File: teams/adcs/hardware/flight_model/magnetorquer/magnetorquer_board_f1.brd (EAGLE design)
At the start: 90 x 90 mm, 58 parts, among them U5 LTC3624

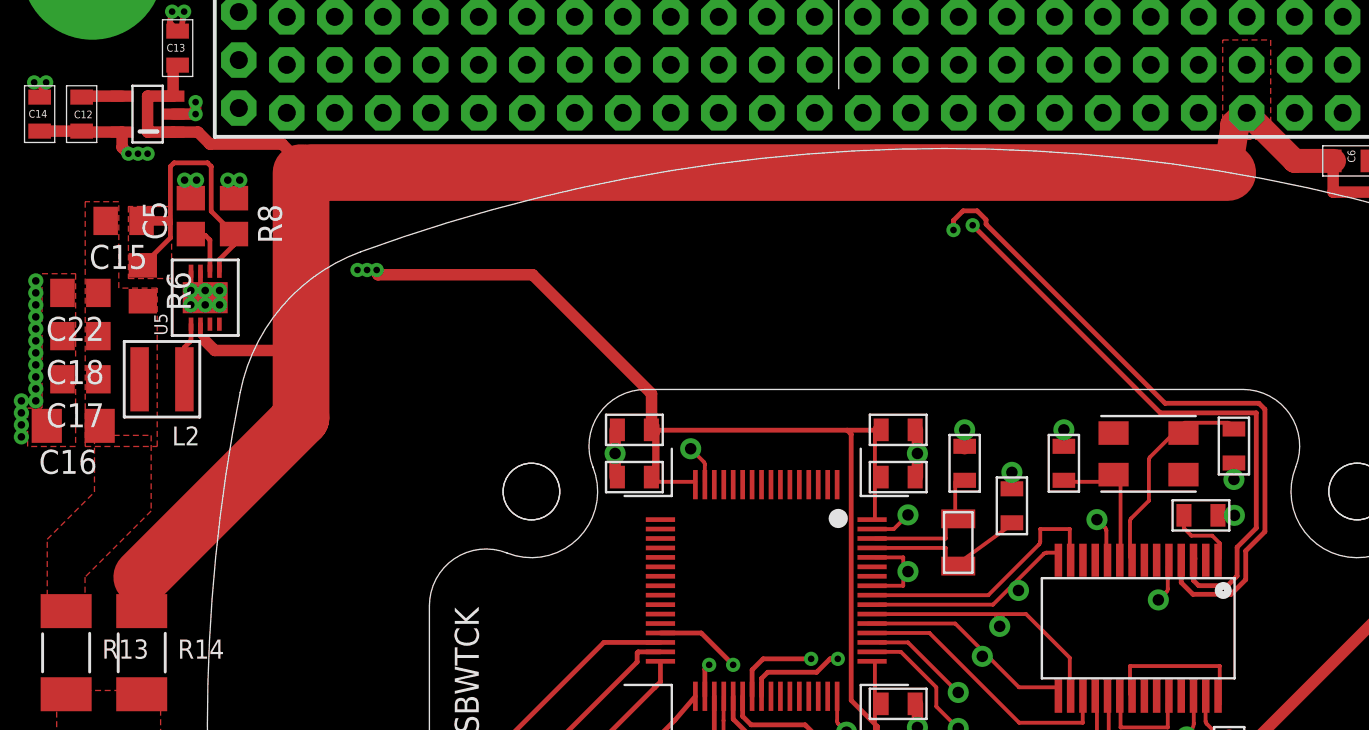
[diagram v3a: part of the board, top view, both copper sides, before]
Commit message: ADCS/MT: Add input capacitance on buck converter
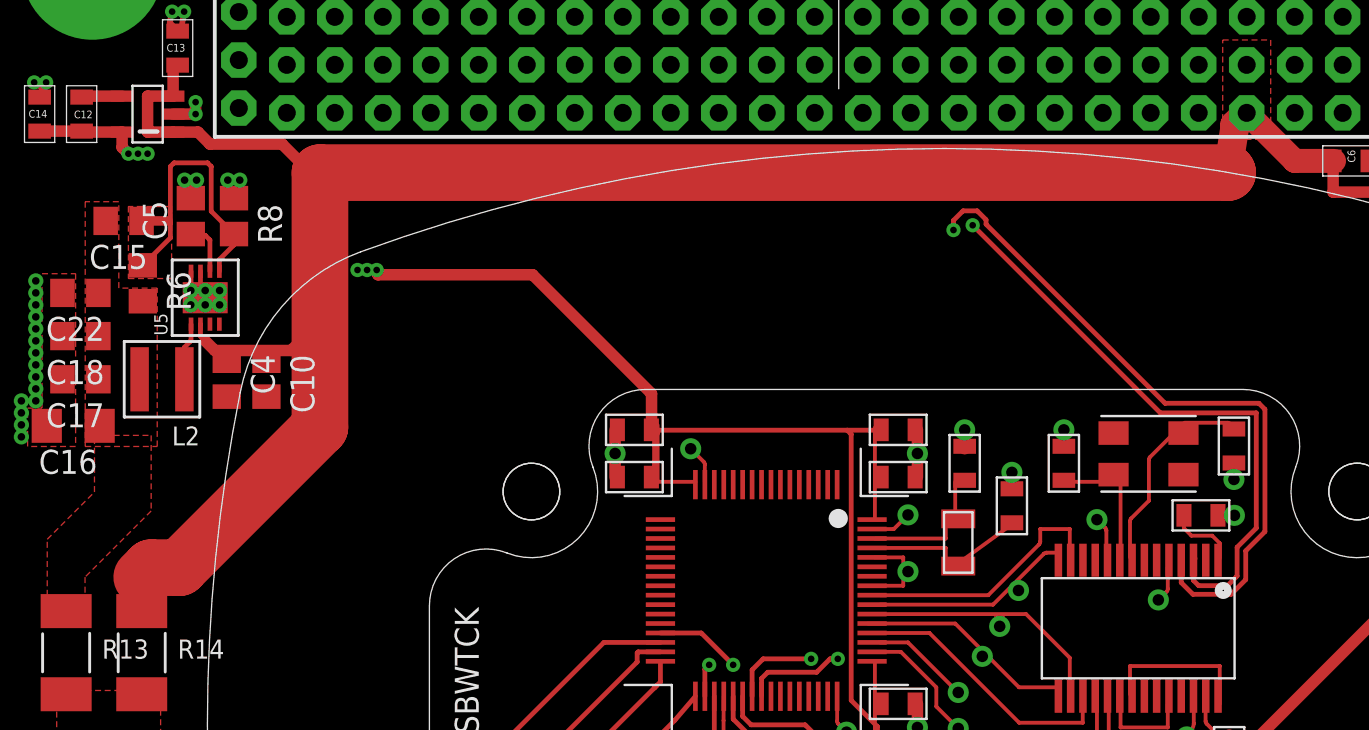
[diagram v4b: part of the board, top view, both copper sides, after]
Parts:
- added C10: 10µF, rcl:C0805
- added C4: 1µF, rcl:C0805
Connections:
- net GND: now also C10.2, C4.2
- net VBAT: now also C10.1, C4.1
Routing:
- net VBAT: track 124.1 -> 126.7 mm
- net +3V3: track 86.1 -> 83.8 mm
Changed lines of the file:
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@@
 <?xml version="1.0" encoding="utf-8"?>
 <!DOCTYPE eagle SYSTEM "eagle.dtd">
-<eagle version="8.4.2">
+<eagle version="9.0.0">
 <drawing>
 <settings>
@@
 <param name="checkRestrict" value="1"/>
 <param name="checkStop" value="0"/>
+<param name="checkValues" value="0"/>
 <param name="useDiameter" value="13"/>
 <param name="maxErrors" value="50"/>
@@
 <element name="R13" library="DubSat1 Components" package="R2010" value="0" x="15.5" y="47" rot="R270"/>
 <element name="R14" library="DubSat1 Components" package="R2010" value="DNP" x="19.5" y="47" rot="R270"/>
+<element name="C4" library="rcl" library_urn="urn:adsk.eagle:library:334" package="C0805" package3d_urn="urn:adsk.eagle:package:23617/2" value="1µF" x="24" y="61.5" rot="R270">
+<attribute name="SPICEPREFIX" value="C" x="24" y="61.5" size="1.778" layer="27" rot="R270" display="off"/>
+</element>
+<element name="C10" library="rcl" library_urn="urn:adsk.eagle:library:334" package="C0805" package3d_urn="urn:adsk.eagle:package:23617/2" value="10µF" x="26.1" y="61.5" rot="R270">
+<attribute name="SPICEPREFIX" value="C" x="26.1" y="61.5" size="1.778" layer="27" rot="R270" display="off"/>
+</element>
 </elements>
 <signals>
@@
 <via x="50.8924" y="31.7584" extent="1-16" drill="0.3" shape="square"/>
 <via x="50.3924" y="31.7584" extent="1-16" drill="0.3" shape="square"/>
+<contactref element="C10" pad="2"/>
+<contactref element="C4" pad="2"/>
 <wire x1="72.5654" y1="31.9347" x2="72.39" y2="31.38" width="0" layer="19" extent="1-1"/>
 <wire x1="62.516" y1="31.174" x2="62.8194" y2="31.1727" width="0" layer="19" extent="1-1"/>
@@
 <wire x1="60.1936" y1="9.2712" x2="60.2436" y2="9.7712" width="0" layer="19" extent="1-1"/>
 <wire x1="44.1936" y1="9.2712" x2="44.2436" y2="9.7712" width="0" layer="19" extent="1-1"/>
+<wire x1="24" y1="60.55" x2="23.622" y2="65.405" width="0" layer="19" extent="1-1"/>
+<wire x1="26.1" y1="60.55" x2="42.1936" y2="4.0212" width="0" layer="19" extent="1-1"/>
 </signal>
 <signal name="N$18">
@@
 <wire x1="77.978" y1="75.568" x2="77.343" y2="74.933" width="1.524" layer="1"/>
 <wire x1="77.343" y1="74.933" x2="77.343" y2="74.77891875" width="1.524" layer="1"/>
-<wire x1="77.343" y1="74.77891875" x2="76.9733" y2="72.40921875" width="1.524" layer="1"/>
-<wire x1="28.43521875" y1="72.40921875" x2="27.932" y2="72.406" width="1.524" layer="1"/>
-<wire x1="76.9733" y1="72.40921875" x2="28.43521875" y2="72.40921875" width="3" layer="1"/>
-<wire x1="26.9304375" y1="73.914" x2="28.43521875" y2="72.40921875" width="0.6096" layer="1"/>
+<wire x1="76.9733" y1="72.40921875" x2="77.343" y2="74.77891875" width="1.524" layer="1"/>
 <wire x1="23.114" y1="73.914" x2="26.9304375" y2="73.914" width="0.6096" layer="1"/>
-<wire x1="27.932" y1="59.432" x2="19.5" y2="51" width="3" layer="1"/>
-<wire x1="27.932" y1="72.406" x2="27.932" y2="59.432" width="3" layer="1"/>
 <contactref element="R14" pad="1"/>
-<wire x1="27.932" y1="59.432" x2="27.408" y2="62.992" width="0" layer="19" extent="1-1"/>
-<wire x1="19.5" y1="49.2" x2="19.5" y2="51" width="0" layer="19" extent="1-1"/>
+<contactref element="C10" pad="1"/>
+<contactref element="C4" pad="1"/>
+<wire x1="21.5" y1="51.5" x2="20" y2="51.5" width="3" layer="1"/>
+<wire x1="28.932" y1="58.932" x2="28.932" y2="72.406" width="3" layer="1"/>
+<wire x1="28.932" y1="58.932" x2="21.5" y2="51.5" width="3" layer="1"/>
+<wire x1="28.932" y1="72.406" x2="76.97008125" y2="72.406" width="3" layer="1"/>
+<wire x1="76.97008125" y1="72.406" x2="76.9733" y2="72.40921875" width="3" layer="1"/>
+<wire x1="26.9304375" y1="73.914" x2="28.4384375" y2="72.406" width="0.6096" layer="1"/>
+<wire x1="28.4384375" y1="72.406" x2="28.932" y2="72.406" width="0.6096" layer="1"/>
+<wire x1="19.5" y1="51" x2="19.5" y2="49.2" width="0.6096" layer="1"/>
+<wire x1="20" y1="51.5" x2="19.5" y2="51" width="3" layer="1"/>
+<wire x1="27.408" y1="62.992" x2="26.1" y2="62.45" width="0" layer="19" extent="1-1"/>
+<wire x1="24" y1="62.45" x2="23.368" y2="62.992" width="0" layer="19" extent="1-1"/>
+<wire x1="28.932" y1="58.932" x2="27.408" y2="62.992" width="0" layer="19" extent="1-1"/>
 </signal>
 <signal name="N$1">
@@
 <wire x1="18.462" y1="74.5515" x2="16.3695" y2="74.5515" width="0.6096" layer="1"/>
 <wire x1="16.3695" y1="74.5515" x2="16.3195" y2="74.6015" width="0.6096" layer="1"/>
-<wire x1="26.416" y1="73.406" x2="28.0695" y2="71.7525" width="0.6096" layer="2"/>
 <wire x1="28.0695" y1="71.7525" x2="31.9355" y2="67.2525" width="0.6096" layer="2"/>
 <via x="31.9355" y="67.2525" extent="1-16" drill="0.35"/>
@@
 <via x="30.9195" y="67.2525" extent="1-16" drill="0.35"/>
 <wire x1="71.4276" y1="41.417" x2="74.5776" y2="54.267" width="0" layer="19" extent="1-1"/>
-<wire x1="69.5325" y1="41.275" x2="69.4276" y2="41.417" width="0" layer="19" extent="1-1"/>
+<wire x1="69.596" y1="41.2115" x2="71.4276" y2="41.417" width="0" layer="19" extent="1-1"/>
 <wire x1="31.4275" y1="67.2525" x2="31.9355" y2="67.2525" width="0" layer="19" extent="1-1"/>
 <wire x1="30.9195" y1="67.2525" x2="31.4275" y2="67.2525" width="0" layer="19" extent="1-1"/>
+<wire x1="26.416" y1="73.406" x2="28.0695" y2="71.7525" width="0" layer="19" extent="2-2"/>
 <wire x1="19.304" y1="73.406" x2="18.796" y2="73.406" width="0" layer="19" extent="1-2"/>
 <wire x1="19.812" y1="73.406" x2="19.304" y2="73.406" width="0" layer="19" extent="1-1"/>

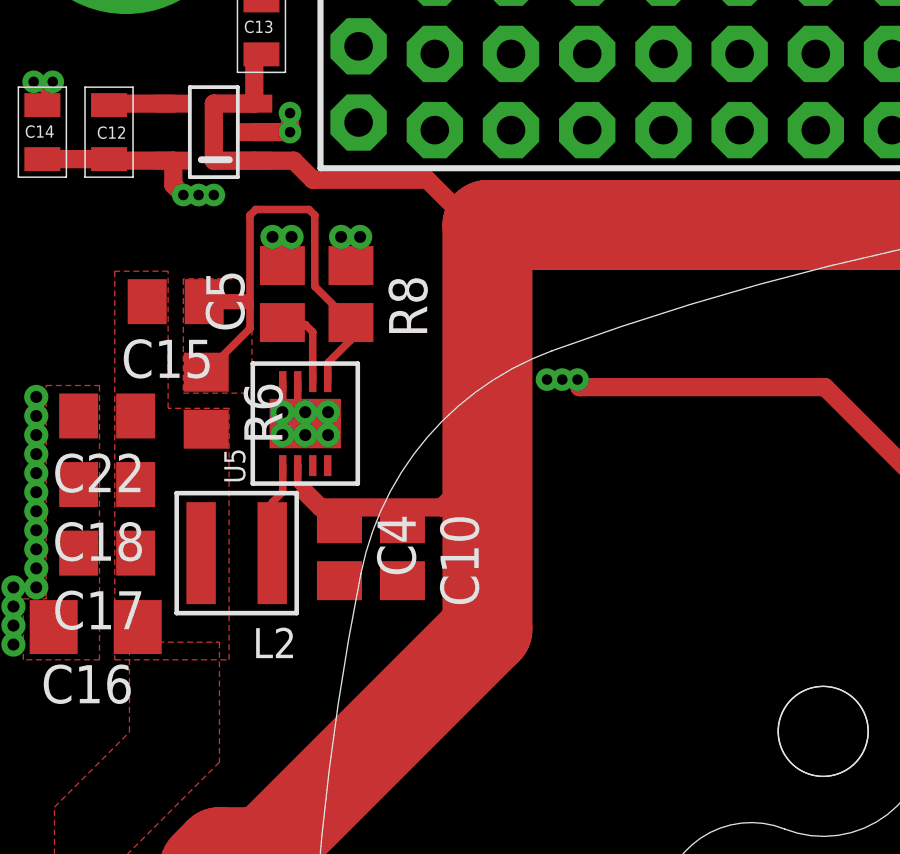
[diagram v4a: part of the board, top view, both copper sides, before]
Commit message: ADCS/MT: Routing to accomodate new buck input capacitors
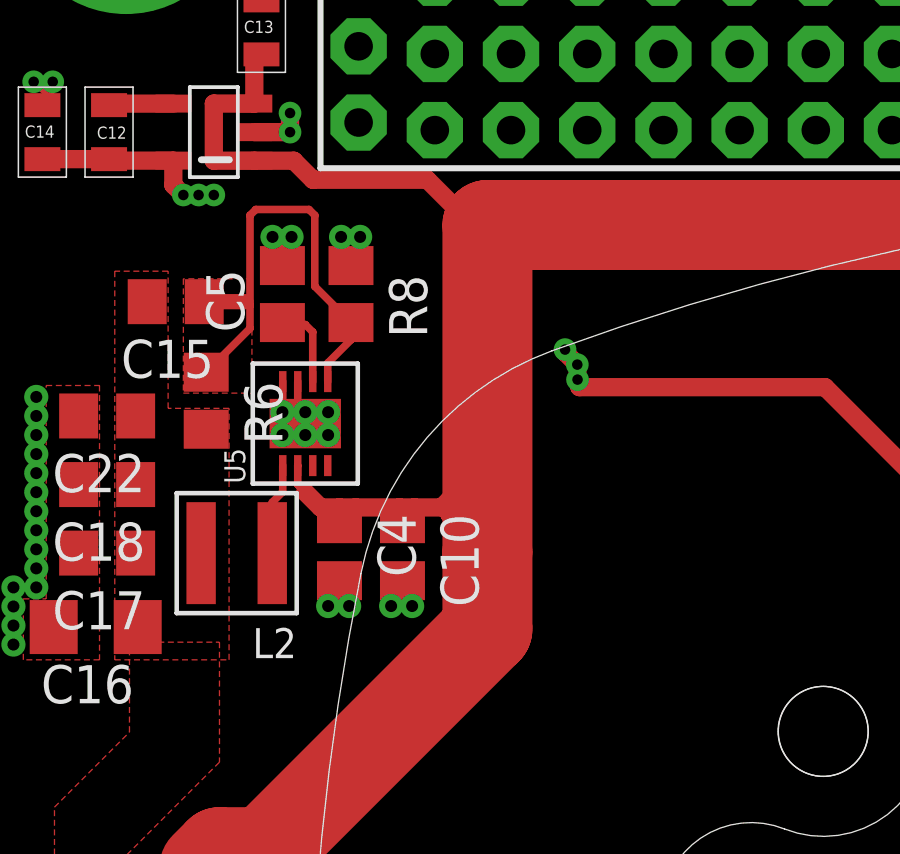
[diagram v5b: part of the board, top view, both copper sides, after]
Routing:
- net VBAT: track 126.7 -> 131.5 mm
- net +3V3: track 83.8 -> 88.0 mm
- net GND: track 66.4 -> 70.3 mm, vias 162 -> 166
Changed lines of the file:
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@@
 <contactref element="C10" pad="2"/>
 <contactref element="C4" pad="2"/>
+<via x="23.622" y="59.705" extent="1-16" drill="0.4" shape="octagon"/>
+<via x="24.322" y="59.705" extent="1-16" drill="0.4" shape="octagon"/>
+<via x="25.722" y="59.705" extent="1-16" drill="0.4" shape="octagon"/>
+<via x="26.422" y="59.705" extent="1-16" drill="0.4" shape="octagon"/>
+<wire x1="23.622" y1="59.705" x2="23.622" y2="60.172" width="0.6096" layer="1"/>
+<wire x1="23.622" y1="60.172" x2="24" y2="60.55" width="0.6096" layer="1"/>
+<wire x1="24.322" y1="59.705" x2="24" y2="60.027" width="0.6096" layer="1"/>
+<wire x1="24" y1="60.027" x2="24" y2="60.55" width="0.6096" layer="1"/>
+<wire x1="25.722" y1="59.705" x2="25.722" y2="60.172" width="0.6096" layer="1"/>
+<wire x1="25.722" y1="60.172" x2="26.025" y2="60.475" width="0.6096" layer="1"/>
+<wire x1="26.025" y1="60.475" x2="26.1" y2="60.55" width="0.6096" layer="1"/>
+<wire x1="26.422" y1="59.705" x2="26.025" y2="60.102" width="0.6096" layer="1"/>
+<wire x1="26.025" y1="60.102" x2="26.025" y2="60.475" width="0.6096" layer="1"/>
 <wire x1="72.5654" y1="31.9347" x2="72.39" y2="31.38" width="0" layer="19" extent="1-1"/>
 <wire x1="62.516" y1="31.174" x2="62.8194" y2="31.1727" width="0" layer="19" extent="1-1"/>
@@
 <wire x1="60.1936" y1="9.2712" x2="60.2436" y2="9.7712" width="0" layer="19" extent="1-1"/>
 <wire x1="44.1936" y1="9.2712" x2="44.2436" y2="9.7712" width="0" layer="19" extent="1-1"/>
-<wire x1="24" y1="60.55" x2="23.622" y2="65.405" width="0" layer="19" extent="1-1"/>
-<wire x1="26.1" y1="60.55" x2="42.1936" y2="4.0212" width="0" layer="19" extent="1-1"/>
 </signal>
 <signal name="N$18">
@@
 <wire x1="22.479" y1="74.549" x2="21.162" y2="74.549" width="0.6096" layer="1"/>
 <wire x1="22.479" y1="74.549" x2="23.114" y2="73.914" width="0.6096" layer="1"/>
-<wire x1="27.662" y1="63.246" x2="27.408" y2="62.992" width="0.6096" layer="1"/>
-<wire x1="27.408" y1="62.992" x2="23.368" y2="62.992" width="0.6096" layer="1"/>
+<wire x1="27.408" y1="62.992" x2="27.662" y2="63.246" width="0.6096" layer="1"/>
+<wire x1="24.542" y1="62.992" x2="24" y2="62.992" width="0.6096" layer="1"/>
+<wire x1="24" y1="62.992" x2="23.368" y2="62.992" width="0.6096" layer="1"/>
 <wire x1="22.86" y1="63.5" x2="23.368" y2="62.992" width="0.6096" layer="1"/>
 <wire x1="22.61" y1="64.386" x2="22.61" y2="63.75" width="0.254" layer="1"/>
@@
 <contactref element="C4" pad="1"/>
 <wire x1="21.5" y1="51.5" x2="20" y2="51.5" width="3" layer="1"/>
-<wire x1="28.932" y1="58.932" x2="28.932" y2="72.406" width="3" layer="1"/>
+<wire x1="28.932" y1="58.932" x2="28.932" y2="61.5" width="3" layer="1"/>
+<wire x1="28.932" y1="61.5" x2="28.932" y2="72.406" width="3" layer="1"/>
 <wire x1="28.932" y1="58.932" x2="21.5" y2="51.5" width="3" layer="1"/>
 <wire x1="28.932" y1="72.406" x2="76.97008125" y2="72.406" width="3" layer="1"/>
@@
 <wire x1="19.5" y1="51" x2="19.5" y2="49.2" width="0.6096" layer="1"/>
 <wire x1="20" y1="51.5" x2="19.5" y2="51" width="3" layer="1"/>
-<wire x1="27.408" y1="62.992" x2="26.1" y2="62.45" width="0" layer="19" extent="1-1"/>
-<wire x1="24" y1="62.45" x2="23.368" y2="62.992" width="0" layer="19" extent="1-1"/>
-<wire x1="28.932" y1="58.932" x2="27.408" y2="62.992" width="0" layer="19" extent="1-1"/>
+<wire x1="24" y1="62.45" x2="24.542" y2="62.992" width="0.6096" layer="1"/>
+<wire x1="24.542" y1="62.992" x2="26" y2="62.992" width="0.6096" layer="1"/>
+<wire x1="26" y1="62.992" x2="26.5" y2="62.992" width="0.6096" layer="1"/>
+<wire x1="26.5" y1="62.992" x2="27.408" y2="62.992" width="0.6096" layer="1"/>
+<wire x1="24" y1="62.45" x2="24" y2="62.992" width="0.6096" layer="1"/>
+<wire x1="26.1" y1="62.45" x2="26" y2="62.55" width="0.6096" layer="1"/>
+<wire x1="26" y1="62.55" x2="26" y2="62.992" width="0.6096" layer="1"/>
+<wire x1="26.1" y1="62.45" x2="26.5" y2="62.85" width="0.6096" layer="1"/>
+<wire x1="26.5" y1="62.85" x2="26.5" y2="62.992" width="0.6096" layer="1"/>
+<wire x1="27.662" y1="63.246" x2="27.662" y2="62.77" width="0.6096" layer="1"/>
+<wire x1="27.662" y1="62.77" x2="28.932" y2="61.5" width="0.6096" layer="1"/>
 </signal>
 <signal name="N$1">
@@
 <wire x1="46.482" y1="60.706" x2="46.482" y2="58.833" width="0.6096" layer="1"/>
 <via x="18.796" y="73.406" extent="1-16" drill="0.35"/>
-<wire x1="26.416" y1="73.406" x2="18.796" y2="73.406" width="0.6096" layer="2"/>
+<wire x1="18.796" y1="73.406" x2="26.416" y2="73.406" width="0.6096" layer="2"/>
 <wire x1="18.796" y1="73.406" x2="18.462" y2="73.74" width="0.6096" layer="1"/>
 <wire x1="18.462" y1="73.74" x2="18.462" y2="74.5515" width="0.6096" layer="1"/>
 <wire x1="18.462" y1="74.5515" x2="16.3695" y2="74.5515" width="0.6096" layer="1"/>
 <wire x1="16.3695" y1="74.5515" x2="16.3195" y2="74.6015" width="0.6096" layer="1"/>
-<wire x1="28.0695" y1="71.7525" x2="31.9355" y2="67.2525" width="0.6096" layer="2"/>
 <via x="31.9355" y="67.2525" extent="1-16" drill="0.35"/>
 <via x="19.304" y="73.406" extent="1-16" drill="0.35"/>
 <via x="19.812" y="73.406" extent="1-16" drill="0.35"/>
-<via x="31.4275" y="67.2525" extent="1-16" drill="0.35"/>
-<via x="30.9195" y="67.2525" extent="1-16" drill="0.35"/>
+<via x="31.9275" y="67.7525" extent="1-16" drill="0.35"/>
+<via x="31.5195" y="68.2525" extent="1-16" drill="0.35"/>
+<wire x1="26.416" y1="73.406" x2="31.9355" y2="67.8865" width="0.6096" layer="2"/>
+<wire x1="31.9355" y1="67.8865" x2="31.9355" y2="67.2525" width="0.6096" layer="2"/>
+<wire x1="31.5195" y1="68.2525" x2="31.8855" y2="67.8865" width="0.6096" layer="2"/>
+<wire x1="31.8855" y1="67.8865" x2="31.9355" y2="67.8865" width="0.6096" layer="2"/>
+<wire x1="31.9355" y1="67.2525" x2="31.9275" y2="67.2605" width="0.6096" layer="1"/>
+<wire x1="31.9275" y1="67.2605" x2="31.9275" y2="67.7525" width="0.6096" layer="1"/>
+<wire x1="31.9275" y1="67.7525" x2="31.5195" y2="68.1605" width="0.6096" layer="1"/>
+<wire x1="31.5195" y1="68.1605" x2="31.5195" y2="68.2525" width="0.6096" layer="1"/>
 <wire x1="71.4276" y1="41.417" x2="74.5776" y2="54.267" width="0" layer="19" extent="1-1"/>
 <wire x1="69.596" y1="41.2115" x2="71.4276" y2="41.417" width="0" layer="19" extent="1-1"/>
-<wire x1="31.4275" y1="67.2525" x2="31.9355" y2="67.2525" width="0" layer="19" extent="1-1"/>
-<wire x1="30.9195" y1="67.2525" x2="31.4275" y2="67.2525" width="0" layer="19" extent="1-1"/>
-<wire x1="26.416" y1="73.406" x2="28.0695" y2="71.7525" width="0" layer="19" extent="2-2"/>
 <wire x1="19.304" y1="73.406" x2="18.796" y2="73.406" width="0" layer="19" extent="1-2"/>
 <wire x1="19.812" y1="73.406" x2="19.304" y2="73.406" width="0" layer="19" extent="1-1"/>
